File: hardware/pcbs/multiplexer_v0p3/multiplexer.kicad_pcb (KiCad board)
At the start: 2 copper layers, 82.6 x 88.9 mm, 22 parts, among them K1 CONN_3, M1 VAL**, M2 VAL**, M3 VAL**, P1 CONN_5X2, P2 CONN_5X2, P3 CONN_2, P4 CONN_2, P5 CONN_5X2, U1 ADG44X, U2 ADG44X, U3 ADG44X, U4 ADG44X

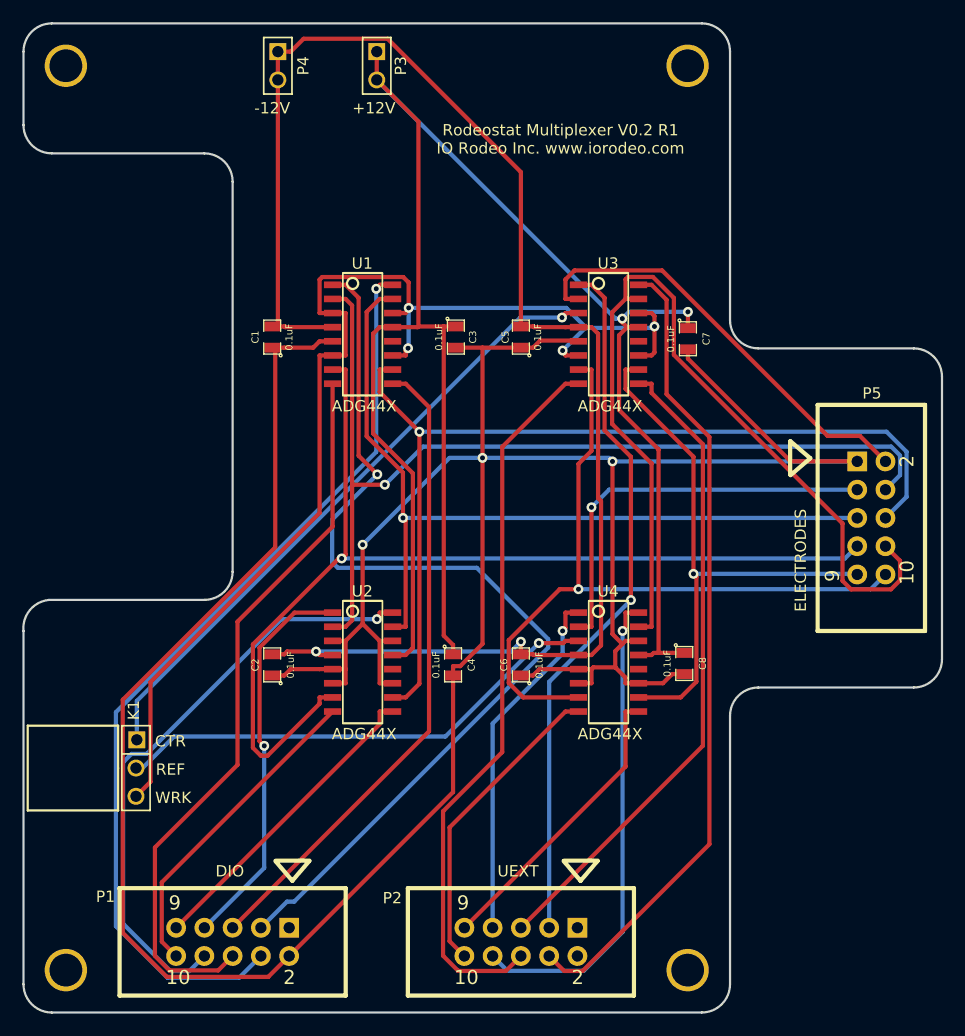
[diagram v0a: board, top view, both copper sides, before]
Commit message: Worked on v0p3 of multiplexer design.
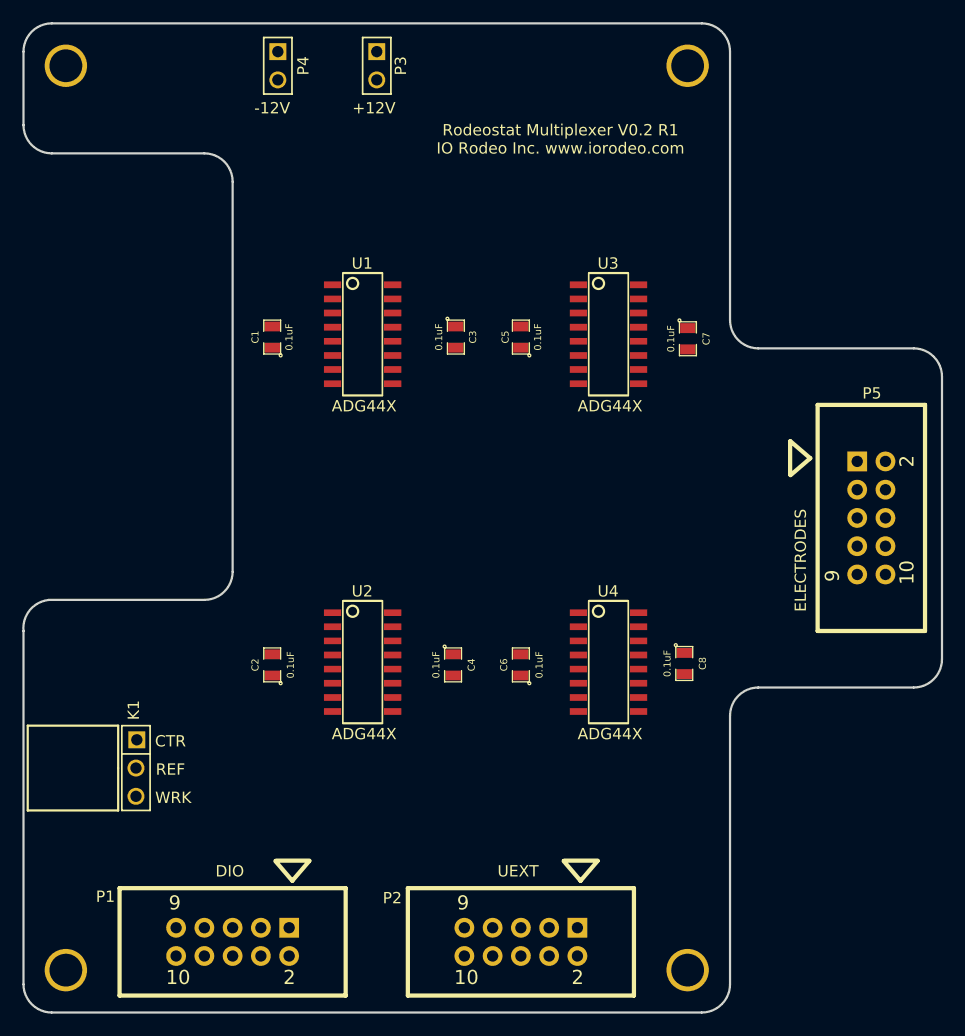
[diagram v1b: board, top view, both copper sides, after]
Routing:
- net /GND: track 292.5 -> 0.00 mm, vias 3 -> 0
- net /+12V: track 171.3 -> 0.00 mm, vias 2 -> 0
- net /-12V: track 139.8 -> 0.00 mm, vias 2 -> 0
- net /WRK: track 109.7 -> 0.00 mm, vias 4 -> 0
- net /WRK_4: track 95.5 -> 0.00 mm, vias 1 -> 0
- net /D24: track 88.3 -> 0.00 mm, vias 1 -> 0
- net /WRK_1: track 86.9 -> 0.00 mm, vias 1 -> 0
- net /WRK_3: track 85.1 -> 0.00 mm, vias 1 -> 0
- net /D25: track 84.4 -> 0.00 mm, vias 1 -> 0
- net /WRK_5: track 81.9 -> 0.00 mm
- net /WRK_2: track 74.6 -> 0.00 mm, vias 1 -> 0
- net /D4: track 73.3 -> 0.00 mm
- net /WRK_7: track 68.3 -> 0.00 mm, vias 1 -> 0
- net /D27: track 66.1 -> 0.00 mm
- net /D18: track 65.3 -> 0.00 mm
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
